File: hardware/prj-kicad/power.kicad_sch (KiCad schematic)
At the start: 15 parts, among them U11 TPS54060A

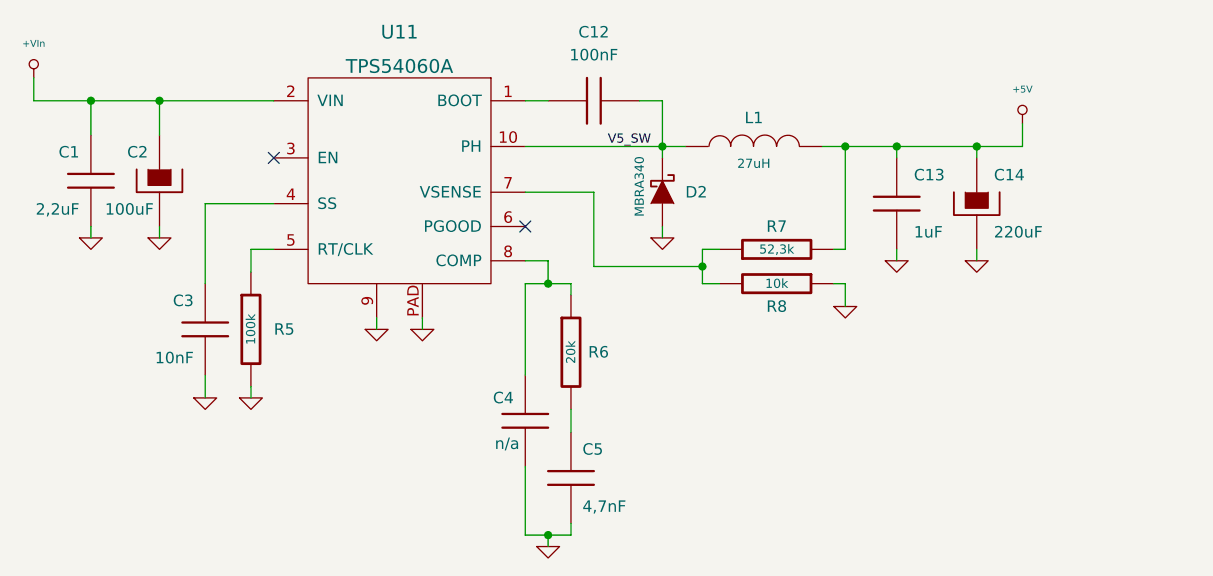
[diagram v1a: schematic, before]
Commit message: Hardware: Finish current sensor interface and create production files for rev1
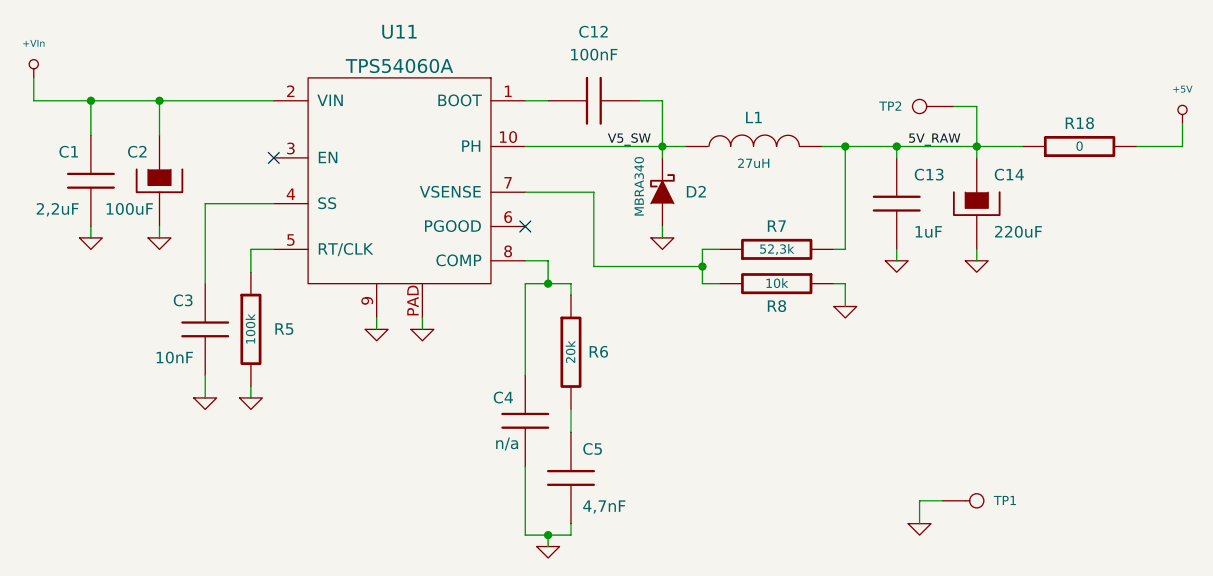
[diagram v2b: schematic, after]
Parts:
- added R18: 0, cowdin-3a-pwrmon:SMD1206, symbol cowdin-3a-pwrmon:R
- added TP1, TP2: CONN_1, cowdin-3a-pwrmon:TP_SMD, symbol cowdin-3a-pwrmon:CONN_1
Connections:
- net +5V: now also R18.2; no longer C13.1, C14.1, L1.2, R7.2
- net GND: now also TP1.1
- new net 5V_RAW: C13.1, C14.1, L1.2, R18.1, R7.2, TP2.1
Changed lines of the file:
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@@
+    (stroke (width 0) (type default) (color 0 0 0 0))
+  )
+  (wire (pts (xy 200.025 81.28) (xy 200.025 78.74))
     (stroke (width 0) (type default) (color 0 0 0 0))
   )
@@
     (stroke (width 0) (type default) (color 0 0 0 0))
   )
+  (wire (pts (xy 170.815 120.65) (xy 173.355 120.65))
+    (stroke (width 0) (type default) (color 0 0 0 0))
+  )
   (wire (pts (xy 86.36 80.01) (xy 86.36 76.2))
     (stroke (width 0) (type default) (color 0 0 0 0))
   )
-  (wire (pts (xy 182.245 78.74) (xy 182.245 81.28))
-    (stroke (width 0) (type default) (color 0 0 0 0))
-  )
   (wire (pts (xy 86.36 76.2) (xy 99.06 76.2))
     (stroke (width 0) (type default) (color 0 0 0 0))
@@
     (stroke (width 0) (type default) (color 0 0 0 0))
   )
+  (wire (pts (xy 174.625 76.835) (xy 177.165 76.835))
+    (stroke (width 0) (type default) (color 0 0 0 0))
+  )
   (wire (pts (xy 78.74 90.17) (xy 78.74 91.44))
     (stroke (width 0) (type default) (color 0 0 0 0))
@@
     (stroke (width 0) (type default) (color 0 0 0 0))
   )
+  (wire (pts (xy 177.165 76.835) (xy 177.165 81.28))
+    (stroke (width 0) (type default) (color 0 0 0 0))
+  )
   (wire (pts (xy 146.685 94.615) (xy 134.62 94.615))
     (stroke (width 0) (type default) (color 0 0 0 0))
@@
   )
   (wire (pts (xy 168.275 81.28) (xy 168.275 82.55))
+    (stroke (width 0) (type default) (color 0 0 0 0))
+  )
+  (wire (pts (xy 194.945 81.28) (xy 200.025 81.28))
+    (stroke (width 0) (type default) (color 0 0 0 0))
+  )
+  (wire (pts (xy 170.815 123.19) (xy 170.815 120.65))
     (stroke (width 0) (type default) (color 0 0 0 0))
   )
@@
     (effects (font (size 1.016 1.016)) (justify right bottom))
   )
+  (label "5V_RAW" (at 169.545 81.28 0)
+    (effects (font (size 1.016 1.016)) (justify left bottom))
+  )
   (symbol (lib_id "cowdin-3a-pwrmon:C") (at 132.08 118.11 0) (unit 1)
     (in_bom yes) (on_board yes)
@@
     )
     (property "Datasheet" "" (id 3) (at 132.08 118.11 0)
+      (effects (font (size 1.524 1.524)))
+    )
+    (pin "1")
+    (pin "2")
+  )
+  (symbol (lib_id "cowdin-3a-pwrmon:R") (at 188.595 81.28 90) (unit 1)
+    (in_bom yes) (on_board yes)
+    (property "Reference" "R18" (id 0) (at 188.595 78.74 90))
+    (property "Value" "0" (id 1) (at 188.595 81.28 90)
+      (effects (font (size 1.016 1.016)))
+    )
+    (property "Footprint" "cowdin-3a-pwrmon:SMD1206" (id 2) (at 188.595 81.28 0)
+      (effects (font (size 1.524 1.524)) hide)
+    )
+    (property "Datasheet" "" (id 3) (at 188.595 81.28 0)
       (effects (font (size 1.524 1.524)))
     )
@@
     (pin "2")
   )
-  (symbol (lib_id "cowdin-3a-pwrmon:+5V") (at 182.245 78.74 0) (unit 1)
-    (in_bom yes) (on_board yes) (fields_autoplaced)
-    (property "Reference" "#PWR0149" (id 0) (at 182.245 79.756 0)
-      (effects (font (size 0.762 0.762)) hide)
-    )
-    (property "Value" "+5V" (id 1) (at 182.245 74.93 0)
+  (symbol (lib_id "cowdin-3a-pwrmon:+5V") (at 200.025 78.74 0) (unit 1)
+    (in_bom yes) (on_board yes) (fields_autoplaced)
+    (property "Reference" "#PWR0149" (id 0) (at 200.025 79.756 0)
+      (effects (font (size 0.762 0.762)) hide)
+    )
+    (property "Value" "+5V" (id 1) (at 200.025 74.93 0)
       (effects (font (size 0.762 0.762)))
     )
-    (property "Footprint" "" (id 2) (at 182.245 78.74 0)
-      (effects (font (size 1.524 1.524)))
-    )
-    (property "Datasheet" "" (id 3) (at 182.245 78.74 0)
+    (property "Footprint" "" (id 2) (at 200.025 78.74 0)
+      (effects (font (size 1.524 1.524)))
+    )
+    (property "Datasheet" "" (id 3) (at 200.025 78.74 0)
       (effects (font (size 1.524 1.524)))
     )
@@
     (pin "2")
   )
+  (symbol (lib_id "cowdin-3a-pwrmon:GND") (at 170.815 123.19 0) (unit 1)
+    (in_bom yes) (on_board yes) (fields_autoplaced)
+    (property "Reference" "#PWR0175" (id 0) (at 170.815 123.19 0)
+      (effects (font (size 0.762 0.762)) hide)
+    )
+    (property "Value" "GND" (id 1) (at 170.815 124.968 0)
+      (effects (font (size 0.762 0.762)) hide)
+    )
+    (property "Footprint" "" (id 2) (at 170.815 123.19 0)
+      (effects (font (size 1.524 1.524)))
+    )
+    (property "Datasheet" "" (id 3) (at 170.815 123.19 0)
+      (effects (font (size 1.524 1.524)))
+    )
+    (pin "1")
+  )
   (symbol (lib_id "cowdin-3a-pwrmon:R") (at 132.08 104.14 0) (unit 1)
     (in_bom yes) (on_board yes)
@@
     (pin "1")
     (pin "2")
+  )
+  (symbol (lib_id "cowdin-3a-pwrmon:CONN_1") (at 177.165 120.65 0) (unit 1)
+    (in_bom yes) (on_board yes)
+    (property "Reference" "TP1" (id 0) (at 179.07 120.65 0)
+      (effects (font (size 1.016 1.016)) (justify left))
+    )
+    (property "Value" "CONN_1" (id 1) (at 177.165 119.253 0)
+      (effects (font (size 0.762 0.762)) hide)
+    )
+    (property "Footprint" "cowdin-3a-pwrmon:TP_SMD" (id 2) (at 177.165 120.65 0)
+      (effects (font (size 1.524 1.524)) hide)
+    )
+    (property "Datasheet" "" (id 3) (at 177.165 120.65 0)
+      (effects (font (size 1.524 1.524)))
+    )
+    (pin "1")
   )
   (symbol (lib_id "cowdin-3a-pwrmon:C") (at 78.74 85.09 0) (unit 1)
@@
     (pin "2")
   )
+  (symbol (lib_id "cowdin-3a-pwrmon:CONN_1") (at 170.815 76.835 180) (unit 1)
+    (in_bom yes) (on_board yes)
+    (property "Reference" "TP2" (id 0) (at 168.91 76.835 0)
+      (effects (font (size 1.016 1.016)) (justify left))
+    )
+    (property "Value" "CONN_1" (id 1) (at 170.815 78.232 0)
+      (effects (font (size 0.762 0.762)) hide)
+    )
+    (property "Footprint" "cowdin-3a-pwrmon:TP_SMD" (id 2) (at 170.815 76.835 0)
+      (effects (font (size 1.524 1.524)) hide)
+    )
+    (property "Datasheet" "" (id 3) (at 170.815 76.835 0)
+      (effects (font (size 1.524 1.524)))
+    )
+    (pin "1")
+  )
   (symbol (lib_id "cowdin-3a-pwrmon:C") (at 127 111.76 0) (unit 1)
